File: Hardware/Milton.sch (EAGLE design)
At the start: 81 parts, among them Q1 12MHz, U1 FT231X, U10 SI4464, U3 USD-SOCKETNEW, U4 DDC113TU-7-F, U5 TPS61200, U6 TCR2EE50,LM, U7 MMA8452Q, U8 MAX31850K, U9 BME280, X1 B4B-ZR, X2 M023.5MM, X3 SMA003.062

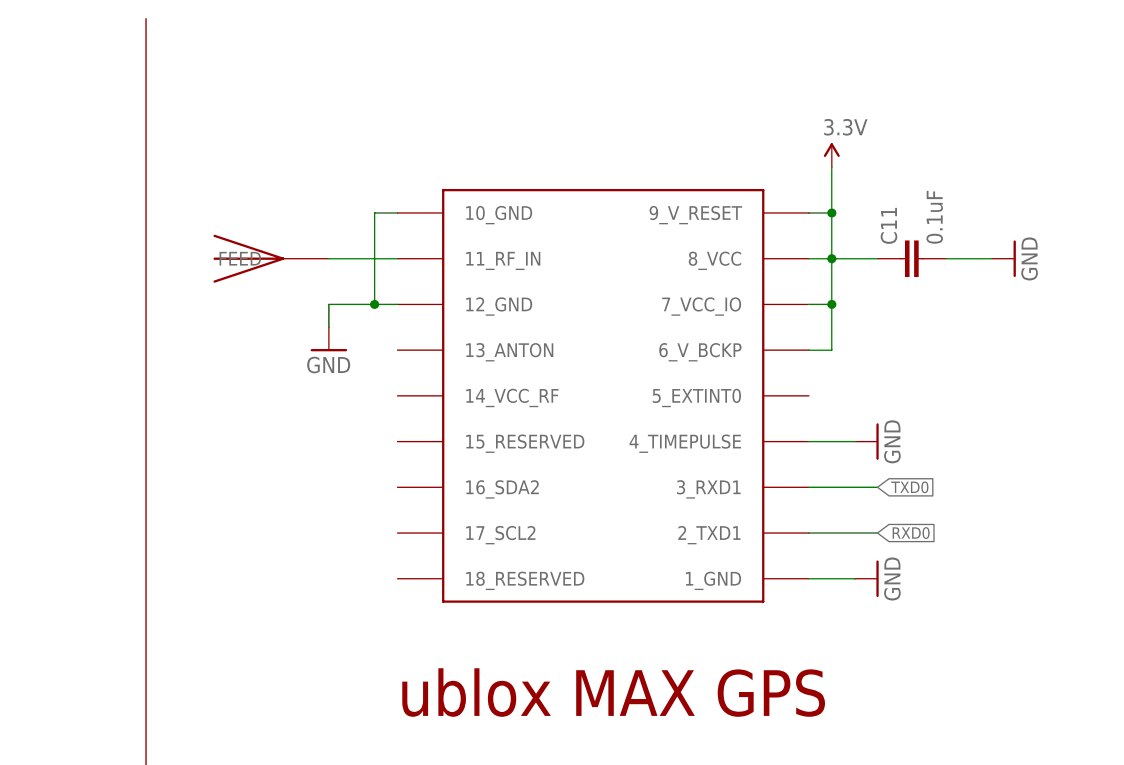
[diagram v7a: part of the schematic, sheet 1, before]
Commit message: Add LED to GPS PPS output
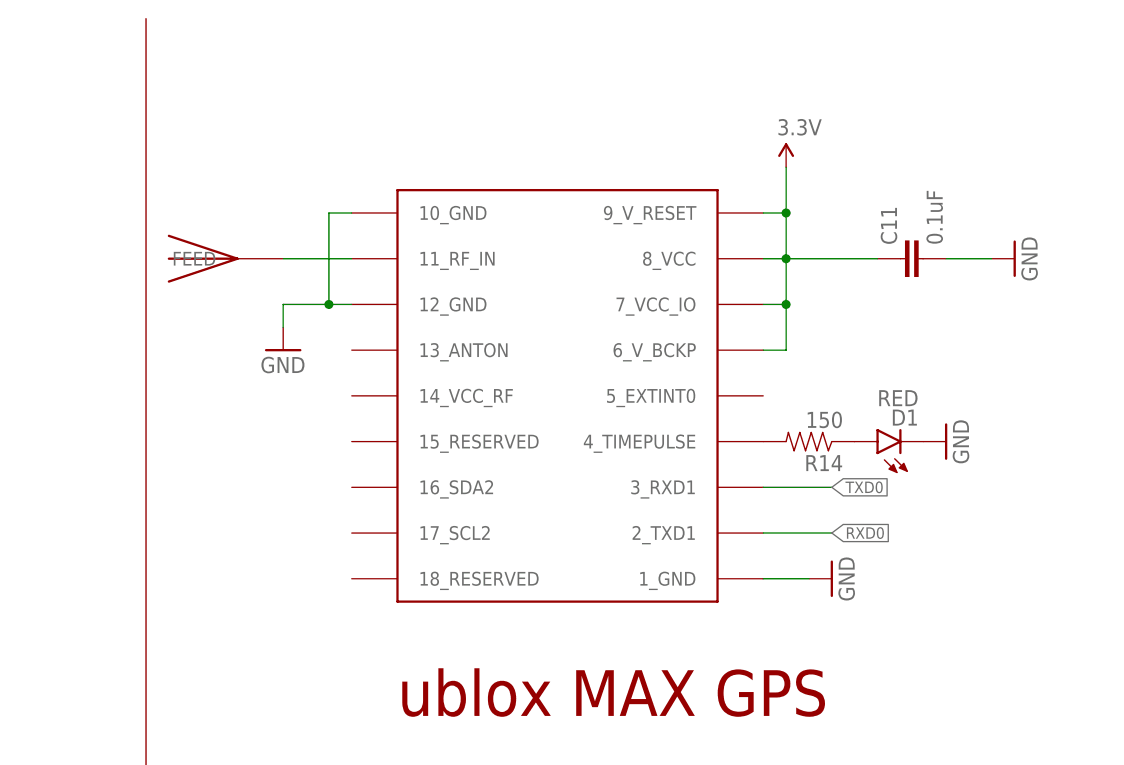
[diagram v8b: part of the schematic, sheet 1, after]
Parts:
- added D1: RED, SparkFun-LED:LED-RED0603
- added R14: 150, SparkFun-Resistors:RESISTOR0603
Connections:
- new net N$16: D1.A, R14.1
- new net N$22: R14.2, U$3.4_TIMEPULSE
- net GND: now also D1.C; no longer U$3.4_TIMEPULSE
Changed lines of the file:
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@@
 <layer number="223" name="223bmp" color="24" fill="1" visible="yes" active="yes"/>
 <layer number="224" name="224bmp" color="25" fill="1" visible="yes" active="yes"/>
+<layer number="225" name="225bmp" color="7" fill="1" visible="yes" active="yes"/>
+<layer number="226" name="226bmp" color="7" fill="1" visible="yes" active="yes"/>
+<layer number="227" name="227bmp" color="7" fill="1" visible="yes" active="yes"/>
+<layer number="228" name="228bmp" color="7" fill="1" visible="yes" active="yes"/>
+<layer number="229" name="229bmp" color="7" fill="1" visible="yes" active="yes"/>
 <layer number="230" name="230bmp" color="7" fill="1" visible="yes" active="yes"/>
 <layer number="231" name="Eagle3D_PG1" color="14" fill="1" visible="yes" active="yes"/>
@@
 <attribute name="MPN" value="CL10B104KO8NNNC"/>
 </part>
-<part name="GND8" library="SparkFun" deviceset="GND" device=""/>
 <part name="U$2" library="ava" deviceset="JTI_ANTENNA-1575AT43A40" device="" value="1575AT43A40">
 <attribute name="MPN" value="1575AT43A0040E"/>
@@
 <part name="FRAME1" library="frames" deviceset="FRAME_B_L" device=""/>
 <part name="FRAME2" library="frames" deviceset="FRAME_A_L" device=""/>
+<part name="D1" library="SparkFun-LED" deviceset="LED-RED" device="0603" value="RED">
+<attribute name="MPN" value="LS L29K-G1J2-1-Z"/>
+</part>
+<part name="R14" library="SparkFun-Resistors" deviceset="RESISTOR" device="0603" value="150">
+<attribute name="MPN" value="ESR03EZPJ151"/>
+</part>
+<part name="GND8" library="SparkFun" deviceset="GND" device=""/>
 </parts>
 <sheets>
@@
 <instance part="P+13" gate="G$1" x="363.22" y="167.64"/>
 <instance part="GND43" gate="1" x="363.22" y="129.54"/>
-<instance part="U$3" gate="G$1" x="375.92" y="238.76">
-<attribute name="MPN" x="375.92" y="238.76" size="1.778" layer="96" display="off"/>
-</instance>
-<instance part="GND2" gate="1" x="406.4" y="213.36" rot="R90"/>
+<instance part="U$3" gate="G$1" x="370.84" y="238.76">
+<attribute name="MPN" x="370.84" y="238.76" size="1.778" layer="96" display="off"/>
+</instance>
+<instance part="GND2" gate="1" x="401.32" y="213.36" rot="R90"/>
 <instance part="GND13" gate="1" x="421.64" y="248.92" rot="R90"/>
 <instance part="C11" gate="G$1" x="411.48" y="248.92" rot="R90">
 <attribute name="MPN" x="411.48" y="248.92" size="1.778" layer="96" rot="R90" display="off"/>
 </instance>
-<instance part="GND8" gate="1" x="406.4" y="228.6" rot="R90"/>
-<instance part="U$2" gate="G$1" x="337.82" y="248.92" rot="R180">
-<attribute name="MPN" x="337.82" y="248.92" size="1.778" layer="96" rot="R180" display="off"/>
-</instance>
-<instance part="SUPPLY12" gate="G$1" x="401.32" y="259.08"/>
+<instance part="U$2" gate="G$1" x="332.74" y="248.92" rot="R180">
+<attribute name="MPN" x="332.74" y="248.92" size="1.778" layer="96" rot="R180" display="off"/>
+</instance>
+<instance part="SUPPLY12" gate="G$1" x="396.24" y="259.08"/>
 <instance part="U2" gate="G$1" x="213.36" y="124.46">
 <attribute name="MPN" x="213.36" y="124.46" size="1.778" layer="96" display="off"/>
@@
 <attribute name="MPN" x="17.78" y="68.58" size="1.27" layer="96" display="off"/>
 </instance>
-<instance part="GND37" gate="1" x="345.44" y="238.76"/>
+<instance part="GND37" gate="1" x="340.36" y="238.76"/>
 <instance part="FRAME1" gate="G$1" x="0" y="0"/>
 <instance part="FRAME1" gate="G$2" x="325.12" y="0"/>
@@
 <attribute name="MPN" x="104.14" y="208.28" size="1.27" layer="96" rot="R90" display="off"/>
 </instance>
+<instance part="D1" gate="G$1" x="406.4" y="228.6" rot="R90">
+<attribute name="MPN" x="406.4" y="228.6" size="2.54" layer="96" rot="R90" display="off"/>
+</instance>
+<instance part="R14" gate="G$1" x="398.78" y="228.6" rot="R180">
+<attribute name="MPN" x="398.78" y="228.6" size="2.54" layer="96" rot="R180" display="off"/>
+</instance>
+<instance part="GND8" gate="1" x="414.02" y="228.6" rot="R90"/>
 </instances>
 <busses>
@@
 <segment>
 <pinref part="U$3" gate="G$1" pin="1_GND"/>
-<wire x1="398.78" y1="213.36" x2="403.86" y2="213.36" width="0.1524" layer="91"/>
+<wire x1="393.7" y1="213.36" x2="398.78" y2="213.36" width="0.1524" layer="91"/>
 <pinref part="GND2" gate="1" pin="GND"/>
 </segment>
@@
 <pinref part="GND13" gate="1" pin="GND"/>
 <pinref part="C11" gate="G$1" pin="2"/>
-</segment>
-<segment>
-<pinref part="U$3" gate="G$1" pin="4_TIMEPULSE"/>
-<pinref part="GND8" gate="1" pin="GND"/>
-<wire x1="403.86" y1="228.6" x2="398.78" y2="228.6" width="0.1524" layer="91"/>
 </segment>
 <segment>
@@
 <segment>
 <pinref part="U$3" gate="G$1" pin="10_GND"/>
-<wire x1="353.06" y1="254" x2="350.52" y2="254" width="0.1524" layer="91"/>
-<wire x1="350.52" y1="254" x2="350.52" y2="243.84" width="0.1524" layer="91"/>
+<wire x1="347.98" y1="254" x2="345.44" y2="254" width="0.1524" layer="91"/>
+<wire x1="345.44" y1="254" x2="345.44" y2="243.84" width="0.1524" layer="91"/>
 <pinref part="U$3" gate="G$1" pin="12_GND"/>
-<wire x1="350.52" y1="243.84" x2="353.06" y2="243.84" width="0.1524" layer="91"/>
-<wire x1="345.44" y1="241.3" x2="345.44" y2="243.84" width="0.1524" layer="91"/>
-<wire x1="345.44" y1="243.84" x2="350.52" y2="243.84" width="0.1524" layer="91"/>
-<junction x="350.52" y="243.84"/>
+<wire x1="345.44" y1="243.84" x2="347.98" y2="243.84" width="0.1524" layer="91"/>
+<wire x1="340.36" y1="241.3" x2="340.36" y2="243.84" width="0.1524" layer="91"/>
+<wire x1="340.36" y1="243.84" x2="345.44" y2="243.84" width="0.1524" layer="91"/>
+<junction x="345.44" y="243.84"/>
 <pinref part="GND37" gate="1" pin="GND"/>
 </segment>
@@
 <pinref part="GND35" gate="1" pin="GND"/>
 </segment>
+<segment>
+<pinref part="D1" gate="G$1" pin="C"/>
+<pinref part="GND8" gate="1" pin="GND"/>
+</segment>
 </net>
 <net name="3.3V" class="5">
@@
 <pinref part="U$3" gate="G$1" pin="9_V_RESET"/>
 <pinref part="U$3" gate="G$1" pin="7_VCC_IO"/>
-<wire x1="398.78" y1="243.84" x2="401.32" y2="243.84" width="0.1524" layer="91"/>
-<wire x1="401.32" y1="243.84" x2="401.32" y2="248.92" width="0.1524" layer="91"/>
-<wire x1="401.32" y1="248.92" x2="401.32" y2="254" width="0.1524" layer="91"/>
-<wire x1="398.78" y1="254" x2="401.32" y2="254" width="0.1524" layer="91"/>
+<wire x1="393.7" y1="243.84" x2="396.24" y2="243.84" width="0.1524" layer="91"/>
+<wire x1="396.24" y1="243.84" x2="396.24" y2="248.92" width="0.1524" layer="91"/>
+<wire x1="396.24" y1="248.92" x2="396.24" y2="254" width="0.1524" layer="91"/>
+<wire x1="393.7" y1="254" x2="396.24" y2="254" width="0.1524" layer="91"/>
 <pinref part="U$3" gate="G$1" pin="8_VCC"/>
-<wire x1="398.78" y1="248.92" x2="401.32" y2="248.92" width="0.1524" layer="91"/>
-<junction x="401.32" y="248.92"/>
-<wire x1="401.32" y1="248.92" x2="406.4" y2="248.92" width="0.1524" layer="91"/>
+<wire x1="393.7" y1="248.92" x2="396.24" y2="248.92" width="0.1524" layer="91"/>
+<junction x="396.24" y="248.92"/>
+<wire x1="396.24" y1="248.92" x2="406.4" y2="248.92" width="0.1524" layer="91"/>
 <pinref part="C11" gate="G$1" pin="1"/>
-<wire x1="401.32" y1="259.08" x2="401.32" y2="254" width="0.1524" layer="91"/>
-<junction x="401.32" y="254"/>
+<wire x1="396.24" y1="259.08" x2="396.24" y2="254" width="0.1524" layer="91"/>
+<junction x="396.24" y="254"/>
 <pinref part="SUPPLY12" gate="G$1" pin="3.3V"/>
 <pinref part="U$3" gate="G$1" pin="6_V_BCKP"/>
-<wire x1="398.78" y1="238.76" x2="401.32" y2="238.76" width="0.1524" layer="91"/>
-<wire x1="401.32" y1="238.76" x2="401.32" y2="243.84" width="0.1524" layer="91"/>
-<junction x="401.32" y="243.84"/>
+<wire x1="393.7" y1="238.76" x2="396.24" y2="238.76" width="0.1524" layer="91"/>
+<wire x1="396.24" y1="238.76" x2="396.24" y2="243.84" width="0.1524" layer="91"/>
+<junction x="396.24" y="243.84"/>
 </segment>
 <segment>
@@
 <pinref part="U$3" gate="G$1" pin="11_RF_IN"/>
 <pinref part="U$2" gate="G$1" pin="FEED"/>
-<wire x1="345.44" y1="248.92" x2="353.06" y2="248.92" width="0.1524" layer="91"/>
+<wire x1="340.36" y1="248.92" x2="347.98" y2="248.92" width="0.1524" layer="91"/>
 </segment>
 </net>
@@
 </segment>
 <segment>
-<wire x1="406.4" y1="218.44" x2="398.78" y2="218.44" width="0.1524" layer="91"/>
-<label x="406.4" y="218.44" size="1.27" layer="95" xref="yes"/>
+<wire x1="401.32" y1="218.44" x2="393.7" y2="218.44" width="0.1524" layer="91"/>
+<label x="401.32" y="218.44" size="1.27" layer="95" xref="yes"/>
 <pinref part="U$3" gate="G$1" pin="2_TXD1"/>
 </segment>
@@
 </segment>
 <segment>
-<wire x1="406.4" y1="223.52" x2="398.78" y2="223.52" width="0.1524" layer="91"/>
-<label x="406.4" y="223.52" size="1.27" layer="95" xref="yes"/>
+<wire x1="401.32" y1="223.52" x2="393.7" y2="223.52" width="0.1524" layer="91"/>
+<label x="401.32" y="223.52" size="1.27" layer="95" xref="yes"/>
 <pinref part="U$3" gate="G$1" pin="3_RXD1"/>
 </segment>
@@
 </segment>
 </net>
+<net name="N$16" class="0">
+<segment>
+<pinref part="D1" gate="G$1" pin="A"/>
+<pinref part="R14" gate="G$1" pin="1"/>
+</segment>
+</net>
+<net name="N$22" class="0">
+<segment>
+<pinref part="U$3" gate="G$1" pin="4_TIMEPULSE"/>
+<pinref part="R14" gate="G$1" pin="2"/>
+</segment>
+</net>
 </nets>
 </sheet>
@@
 <plain>
 <text x="134.62" y="2.54" size="5.08" layer="94">Headers</text>
-<wire x1="5.08" y1="76.2" x2="114.3" y2="76.2" width="0.1524" layer="94"/>
+<wire x1="3.81" y1="76.2" x2="114.3" y2="76.2" width="0.1524" layer="94"/>
 <wire x1="114.3" y1="76.2" x2="172.72" y2="76.2" width="0.1524" layer="94"/>
 <wire x1="172.72" y1="76.2" x2="172.72" y2="35.56" width="0.1524" layer="94"/>
